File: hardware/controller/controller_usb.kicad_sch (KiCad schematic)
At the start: 7 parts, among them J7 USB-C, U4 USBLC6-2SC6

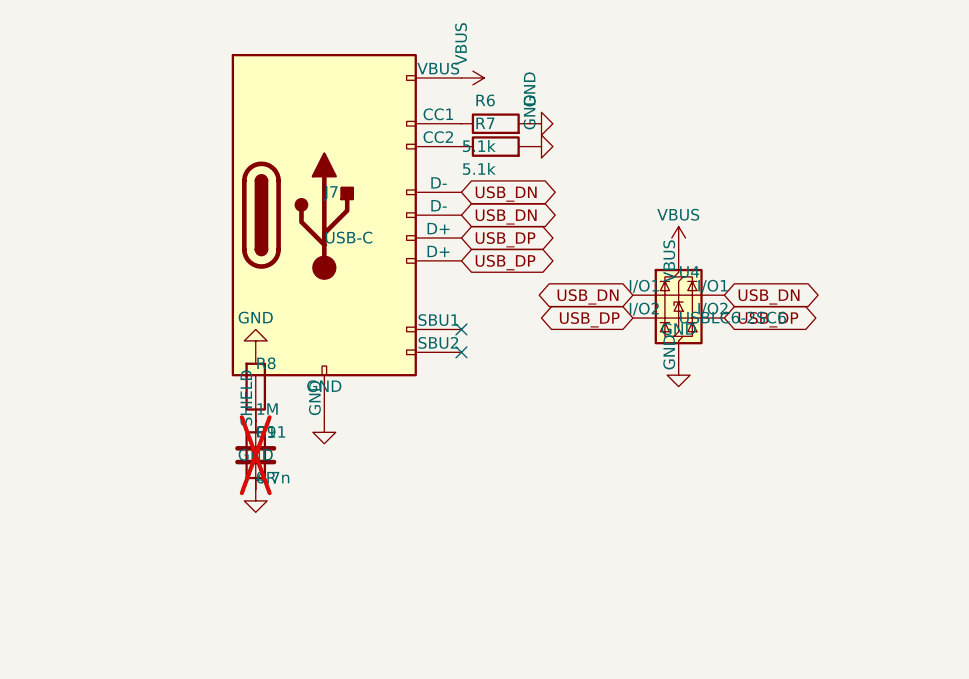
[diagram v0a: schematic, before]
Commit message: feat(hardware): MAX31856 input filter per datasheet, sheet cleanup in progress
- Input filter per MAX31856 "Typical Application Circuit": C14/C17 100 nF
  differential, new C27-C30 10 nF from T+/T- to GND; reference netlist re-exported
- Datasheet checks: BIAS to T- confirmed, FAULT is push-pull (diodes to CLR needed)
- check_schematic.py: sheet format check (raw newline in strings breaks KiCad)
- import_netlist.py: relinks by reference when a symbol gets a new UUID (U7 case)
- Sheets partly rearranged in KiCad by the user (connectivity unchanged, 0 errors)
- MAX31856 order number and price, docs/Component-Specs ignored

Co-Authored-By: Claude Opus 5.5 <noreply@anthropic.com>
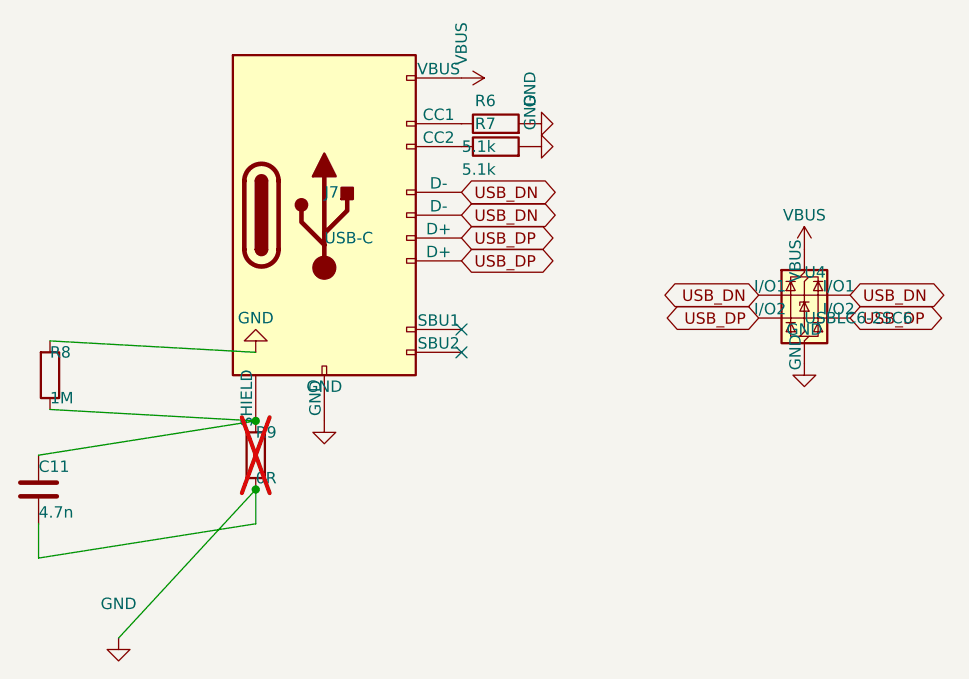
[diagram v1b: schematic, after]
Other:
- moved on the sheet: C11, R8, U4
